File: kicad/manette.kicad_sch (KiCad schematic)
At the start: 31 parts, among them X1 SW_Push, Y1 SW_Push

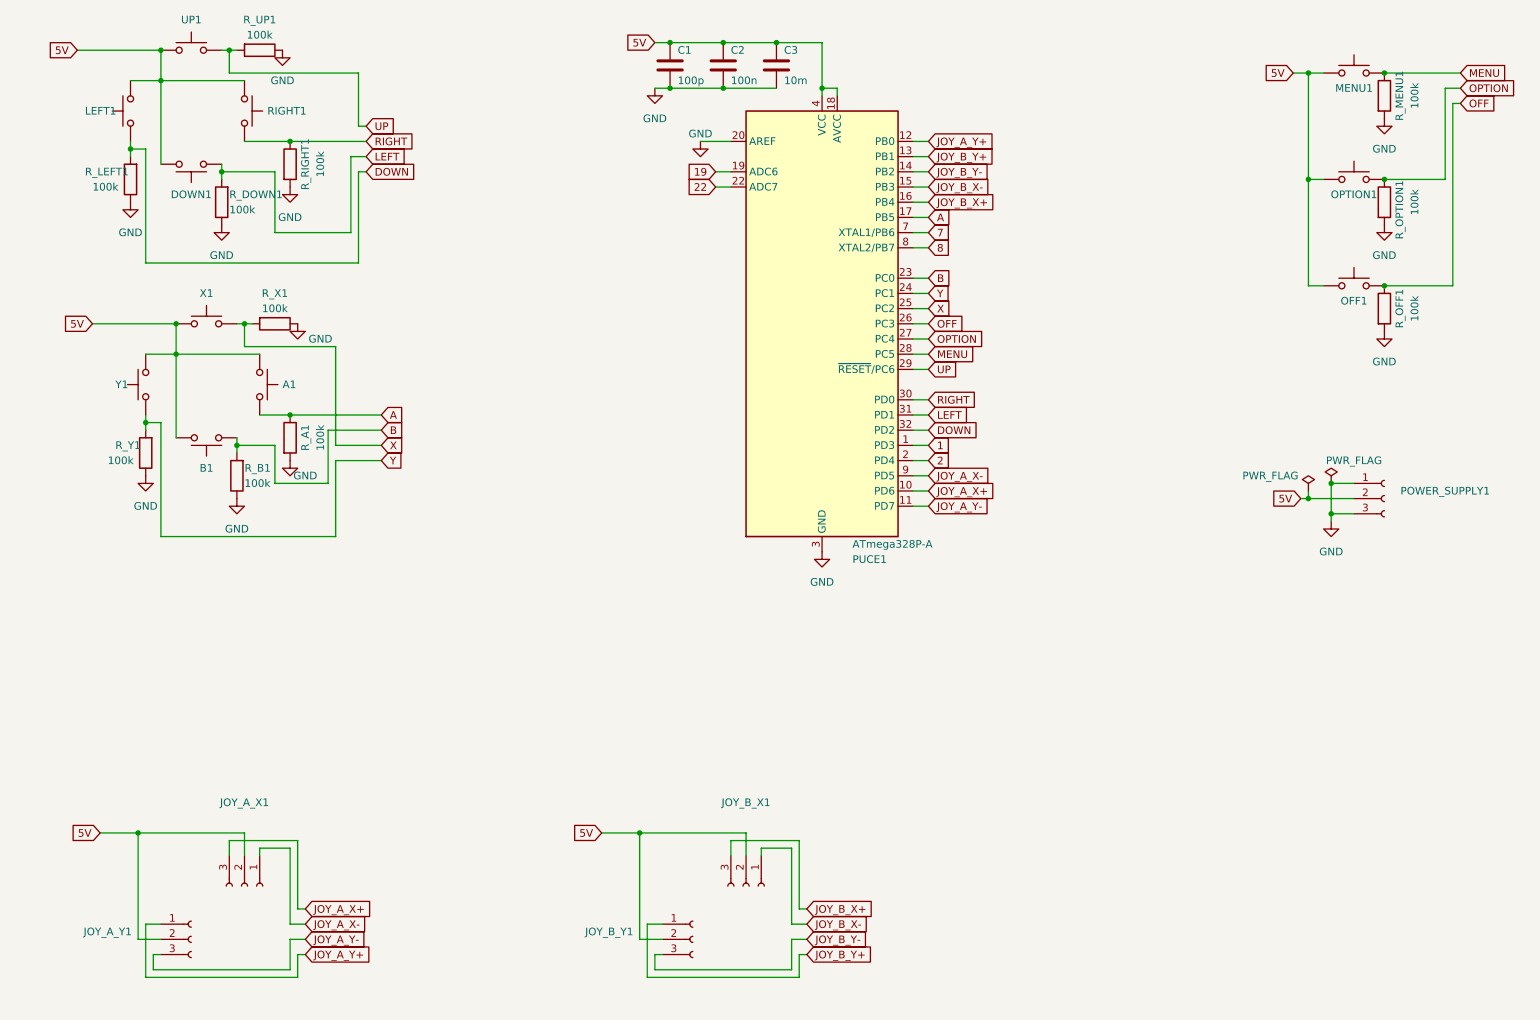
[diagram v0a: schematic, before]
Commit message: ajout d'un joystick achetable
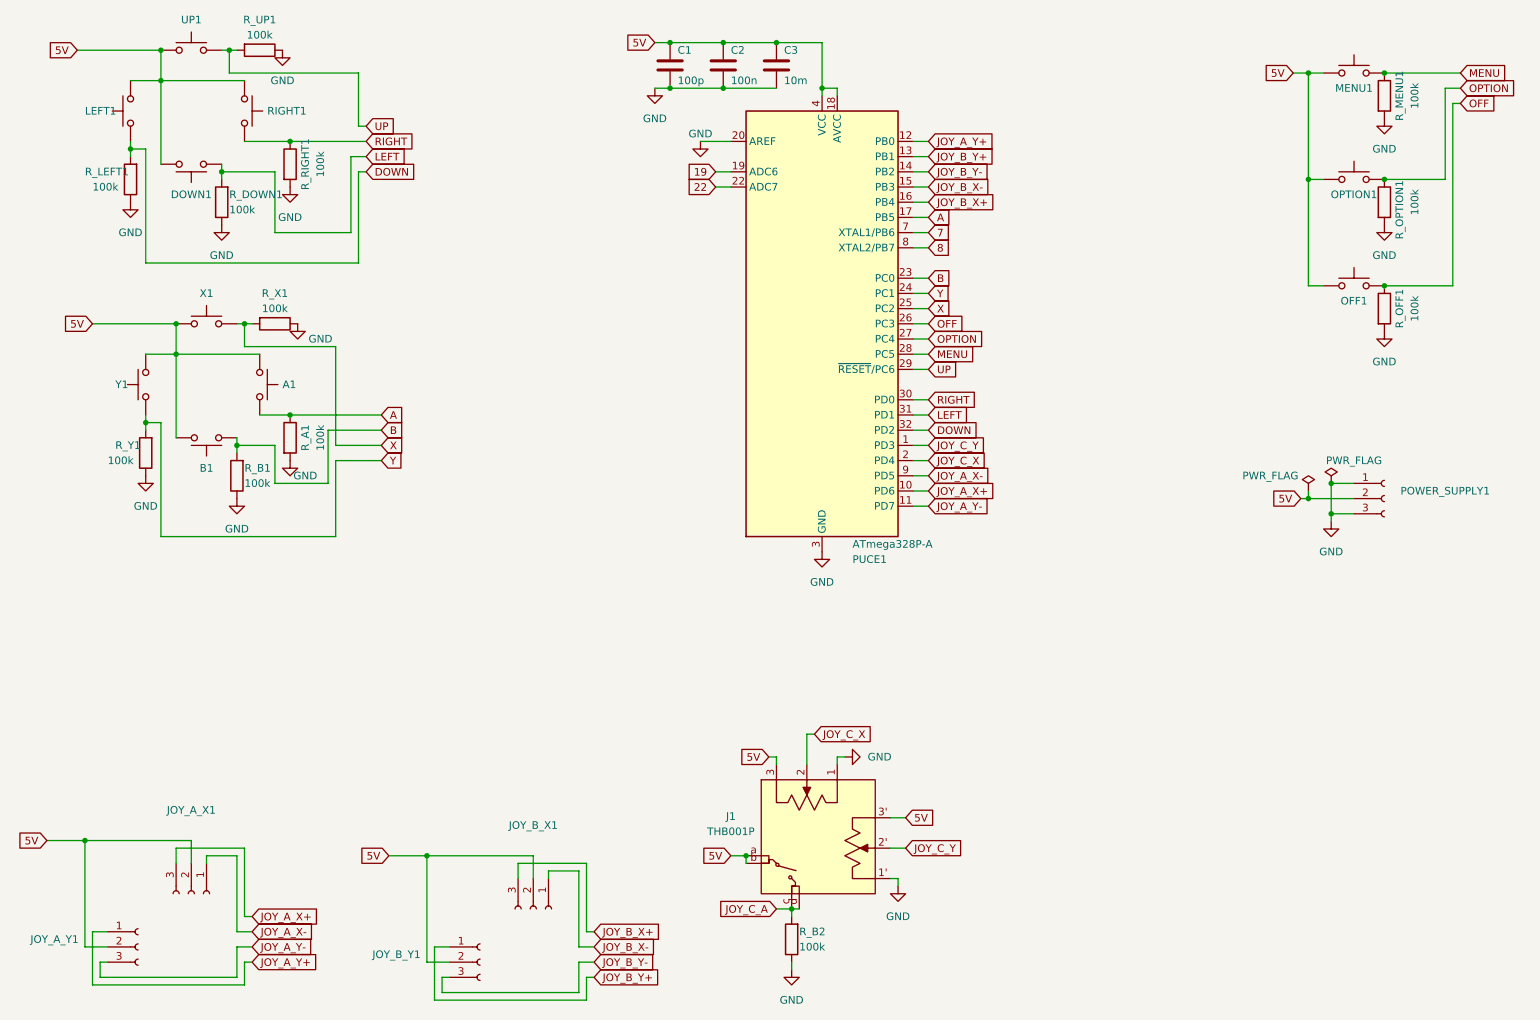
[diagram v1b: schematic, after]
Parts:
- added J1: THB001P, LibPerso:Joystick_THB001P, symbol LibPerso:THB001P
- added R_B2: 100k, Resistor_THT:R_Axial_DIN0411_L9.9mm_D3.6mm_P15.24mm_Horizontal, symbol Device:R
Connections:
- net 5V: now also J1.3, J1.3', J1.a, J1.b
- net GND: now also J1.1, J1.1', R_B2.1
- net 1 renamed JOY_C_Y
- net JOY_C_Y: now also J1.2'
- net 2 renamed JOY_C_X
- net JOY_C_X: now also J1.2
- new net JOY_C_A: J1.c, J1.d, R_B2.2
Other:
- moved on the sheet: JOY_A_X1, JOY_A_Y1, JOY_B_X1, JOY_B_Y1
